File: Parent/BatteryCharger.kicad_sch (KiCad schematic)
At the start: 1 part, among them U31 TSV911IDT

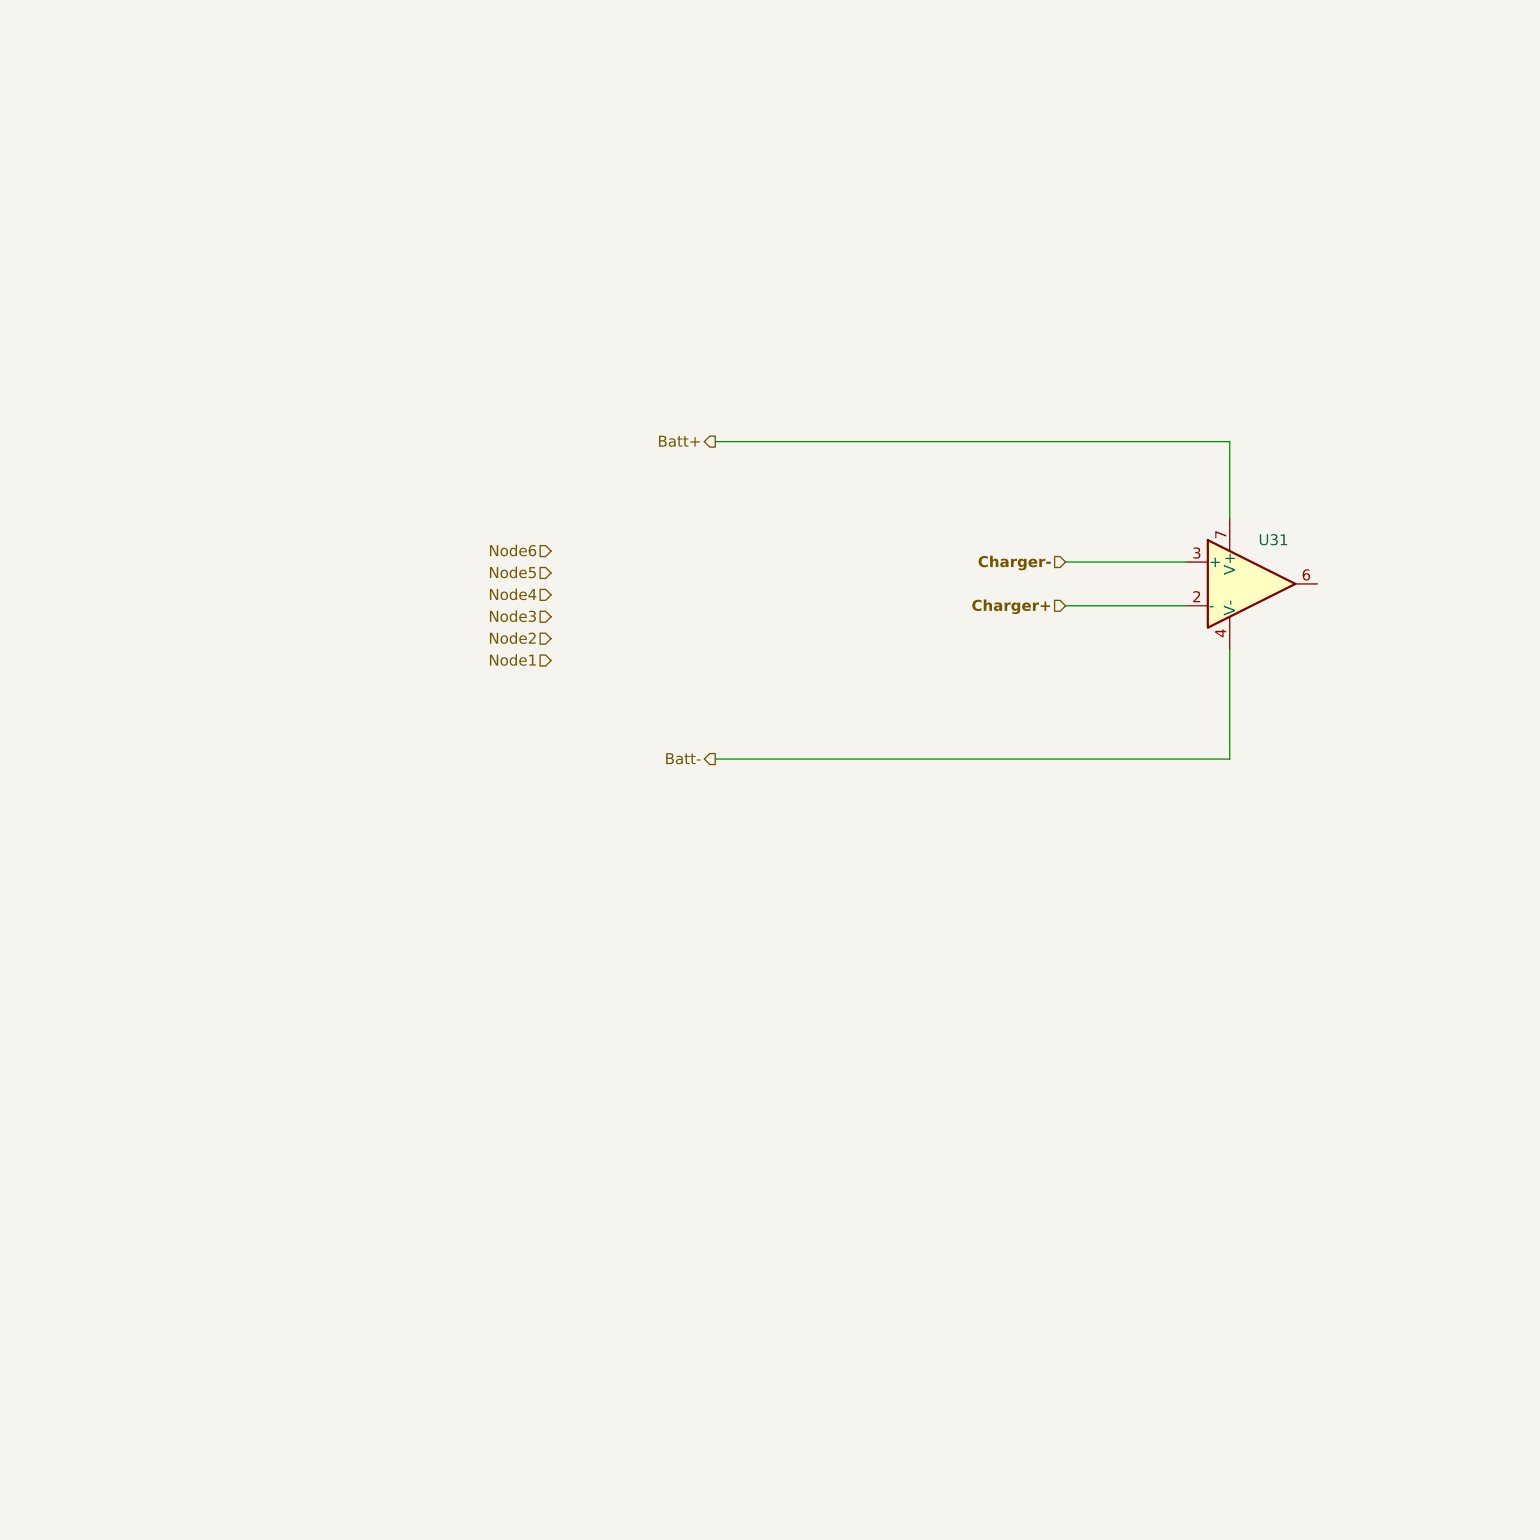
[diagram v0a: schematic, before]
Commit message: Updated Parent further - Move workspace to cloud
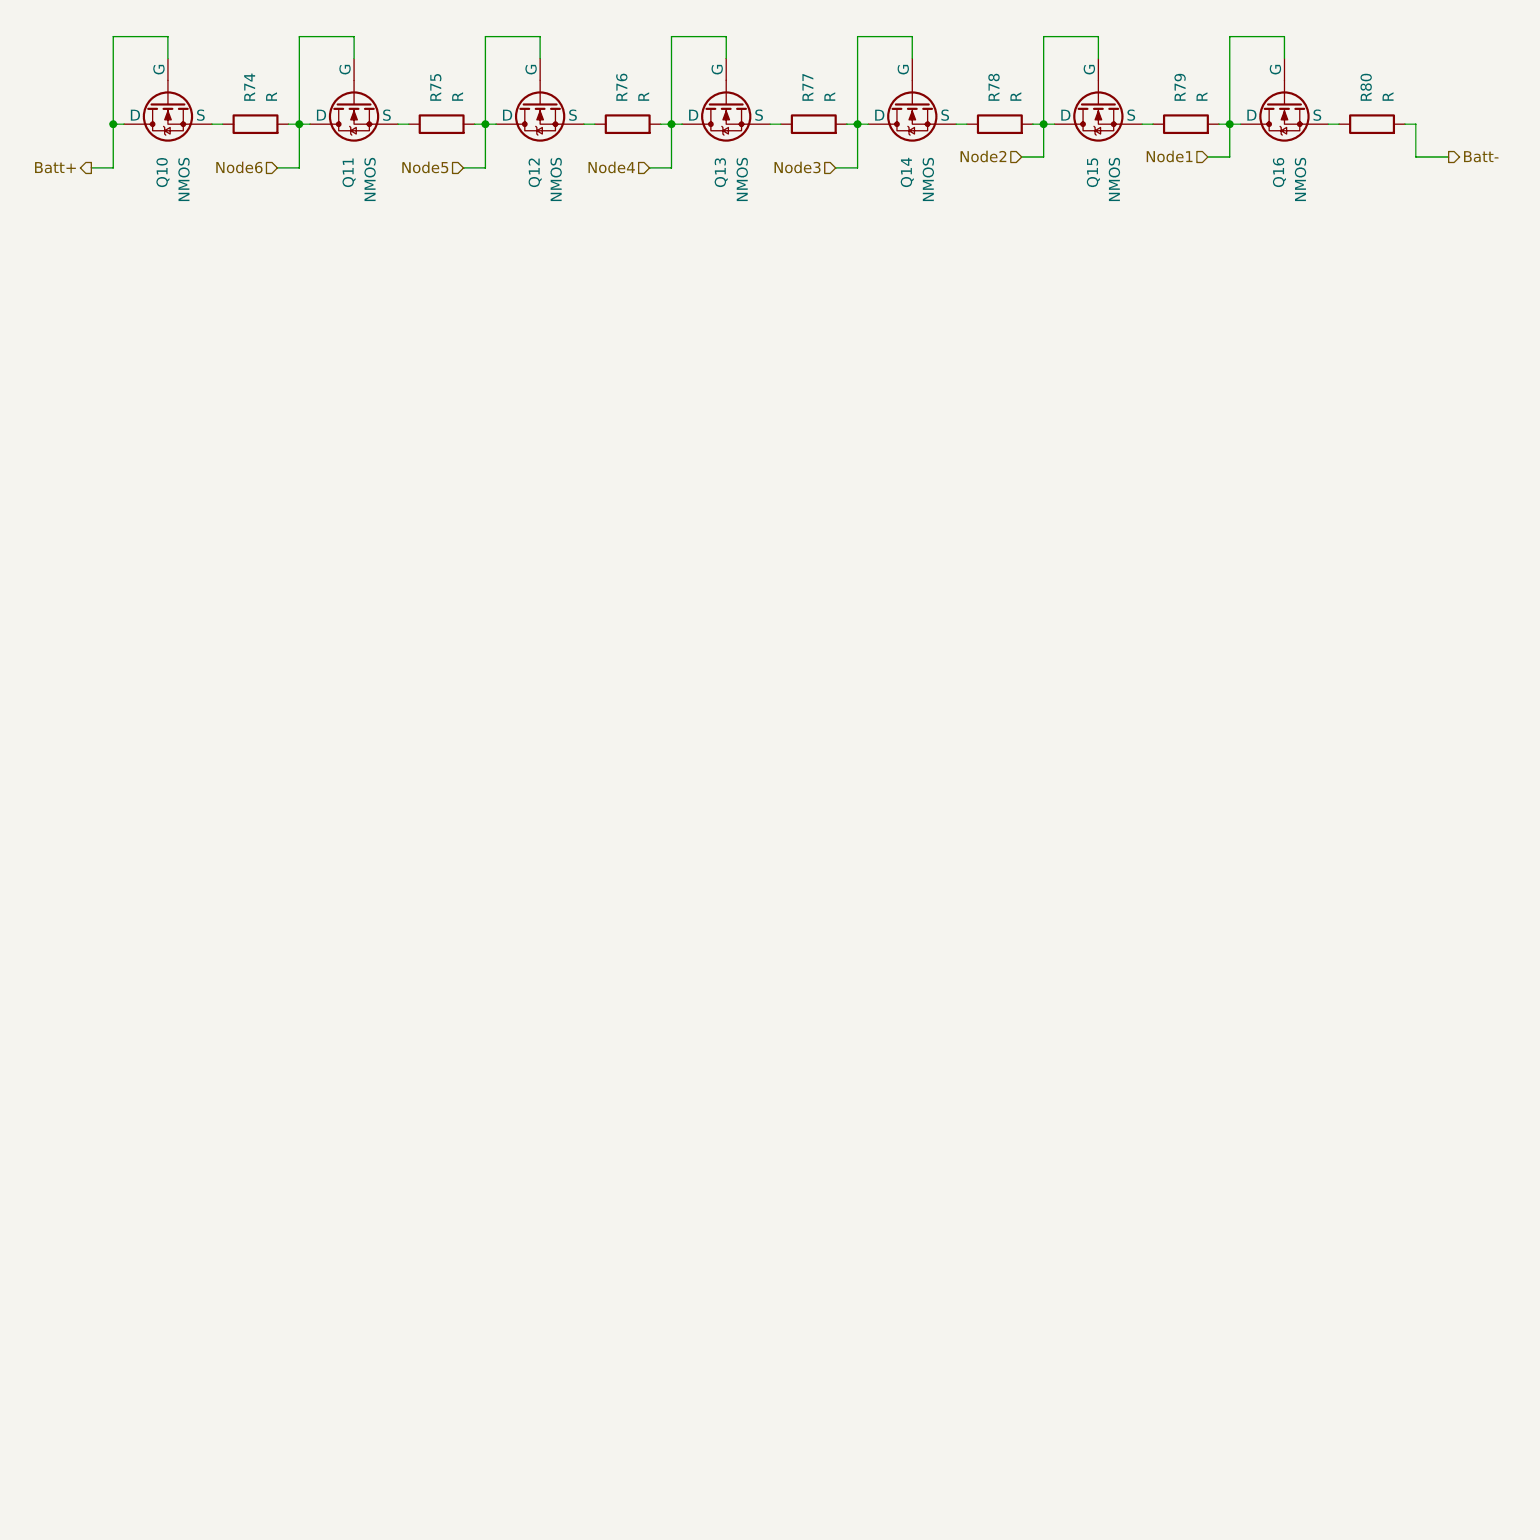
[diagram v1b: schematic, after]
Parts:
- removed U31: TSV911IDT, Package_SO:SOIC-8_3.9x4.9mm_P1.27mm, symbol Amplifier_Operational:TSV911IDT
- added Q10, Q11, Q12, Q13, Q14, Q15, Q16: NMOS, symbol Simulation_SPICE:NMOS
- added R74, R75, R76, R77, R78, R79, R80: R, symbol Device:R
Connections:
- net Batt+: now also Q10.1 (D), Q10.2 (G)
- net Batt-: now also R80.2
- net Node1: now also Q16.1 (D), Q16.2 (G), R79.2
- net Node2: now also Q15.1 (D), Q15.2 (G), R78.2
- net Node3: now also Q14.1 (D), Q14.2 (G), R77.2
- net Node4: now also Q13.1 (D), Q13.2 (G), R76.2
- net Node5: now also Q12.1 (D), Q12.2 (G), R75.2
- net Node6: now also Q11.1 (D), Q11.2 (G), R74.2
- new net: Q11.3 (S), R75.1
- new net: Q10.3 (S), R74.1
- new net: Q16.3 (S), R80.1
- new net: Q13.3 (S), R77.1
- new net: Q14.3 (S), R78.1
- new net: Q12.3 (S), R76.1
- new net: Q15.3 (S), R79.1

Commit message: Updated Parent - Moved workspace to cloud
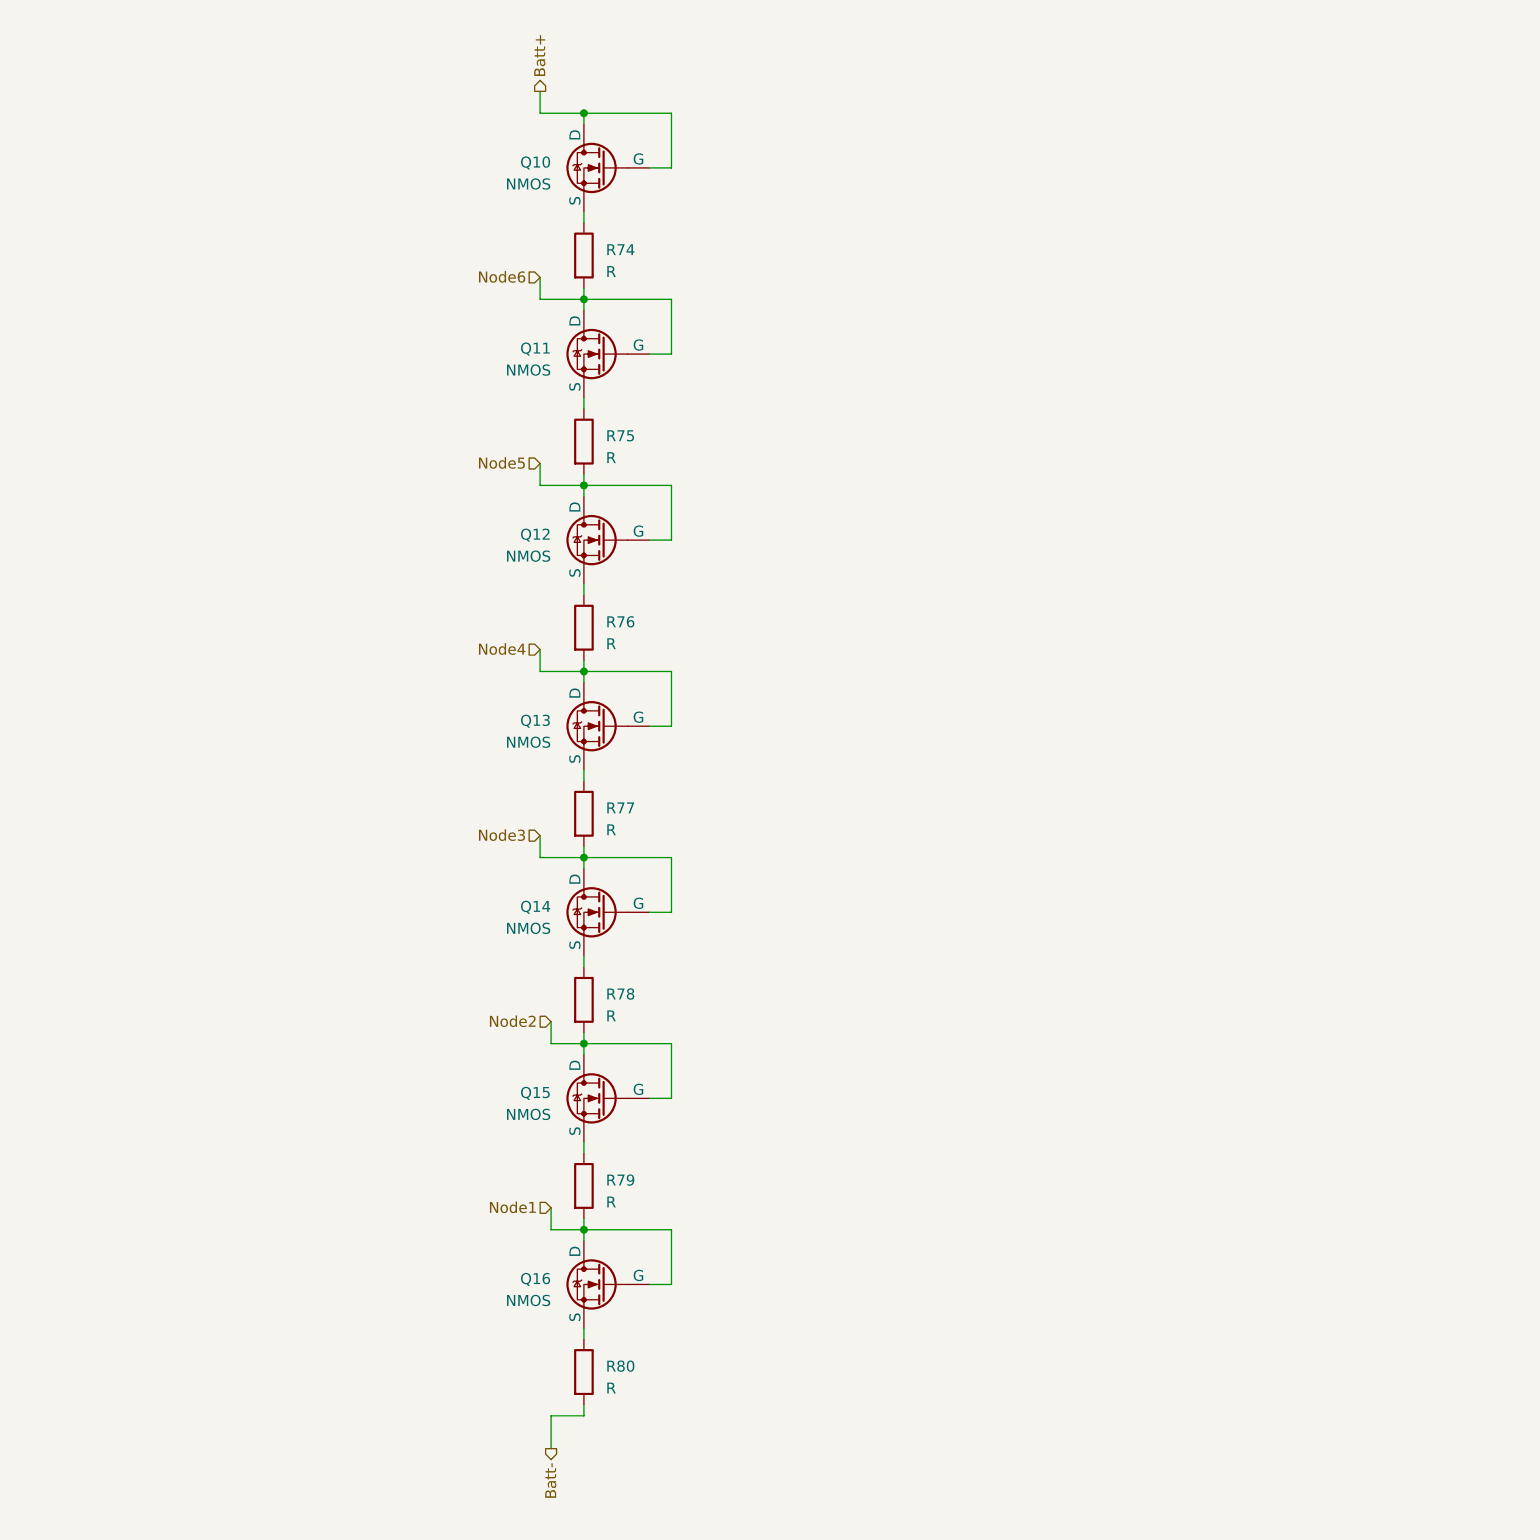
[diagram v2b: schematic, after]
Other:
- moved on the sheet: Q10, Q11, Q12, Q13, Q14, Q15, Q16, R74, R75, R76, R77, R78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
